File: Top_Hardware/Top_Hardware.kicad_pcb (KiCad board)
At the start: 2 copper layers, 15 parts, among them J1 NEO In, J2 Conn_01x03_Female

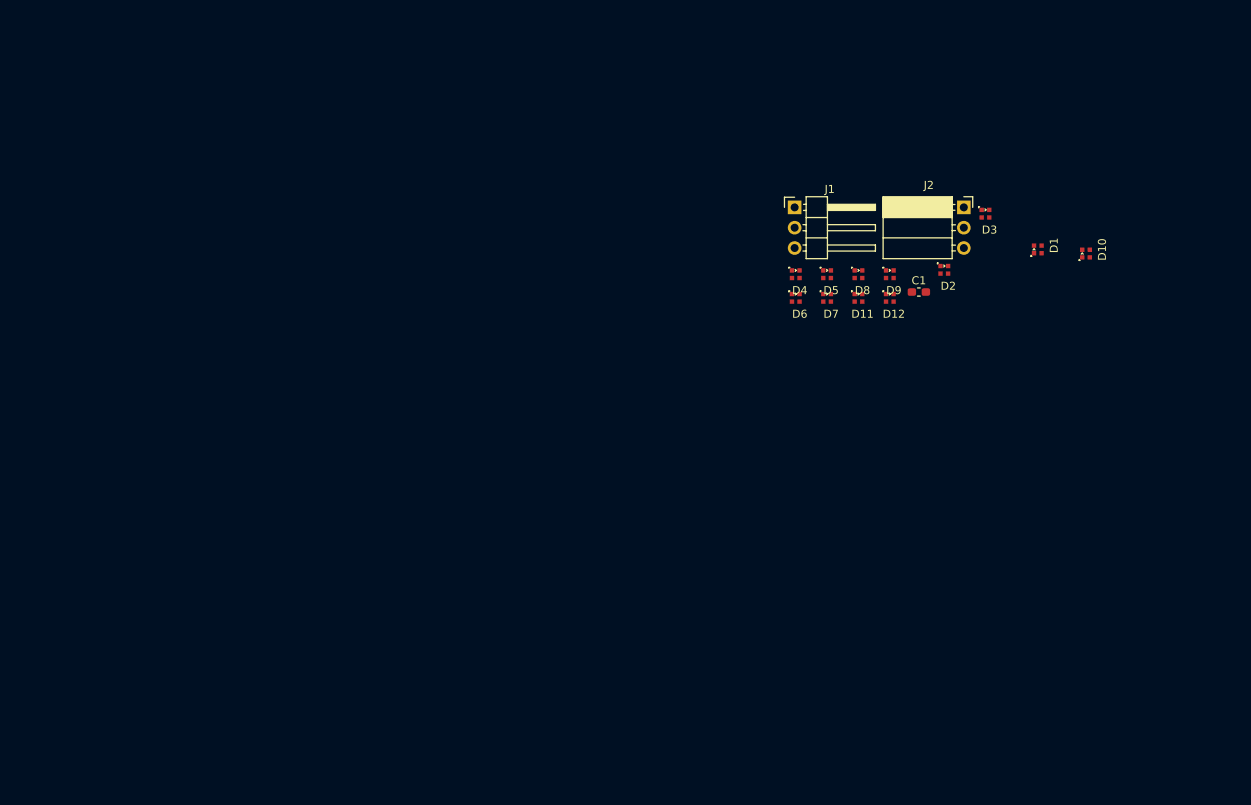
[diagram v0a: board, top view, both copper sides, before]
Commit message: created tree outlines
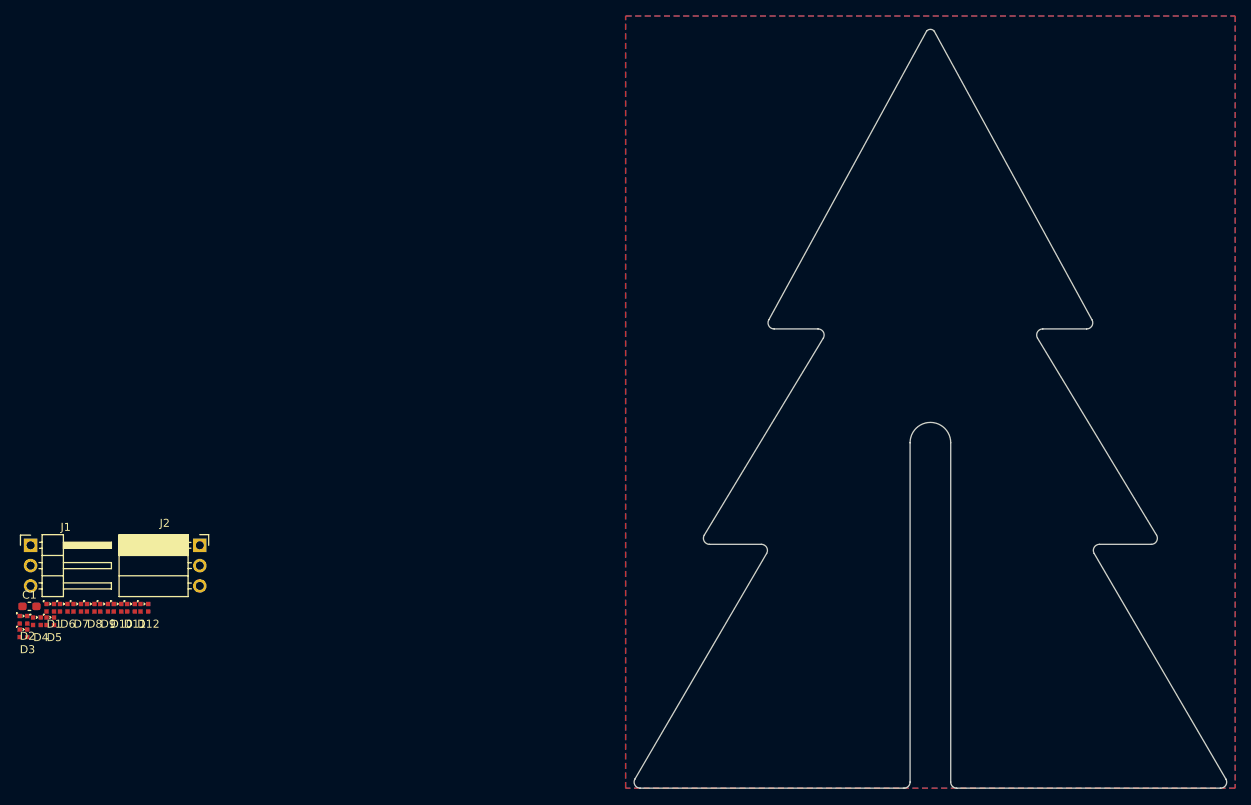
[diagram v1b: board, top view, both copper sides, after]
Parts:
- moved D1 131.3 mm to (32.2, 104.4), turned to 0 degrees
- moved D3 131.2 mm to (28.9, 107.6)
- moved D10 128.9 mm to (40.6, 104.4), turned to 0 degrees
- moved D2 123.1 mm to (28.9, 106.0)
- moved C1 117.9 mm to (29.6, 104.3)
- moved D9 106.7 mm to (38.9, 104.4)
- moved D5 106.3 mm to (32.2, 106.1)
- moved D8 104.6 mm to (37.3, 104.4)
- moved J2 104.4 mm to (50.9, 96.6)
- moved J1 104.4 mm to (29.8, 96.6)
- moved D4 104.3 mm to (30.5, 106.1)
- moved D7 101.4 mm to (35.6, 104.4)
- moved D12 100.9 mm to (44.0, 104.4)
- moved D6 99.4 mm to (33.9, 104.4)
- moved D11 98.8 mm to (42.3, 104.4)
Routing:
- added copper zone on B.Cu, net +5V
- added copper zone on F.Cu, net GND
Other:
- board outline added: 74.1 x 94.8 mm

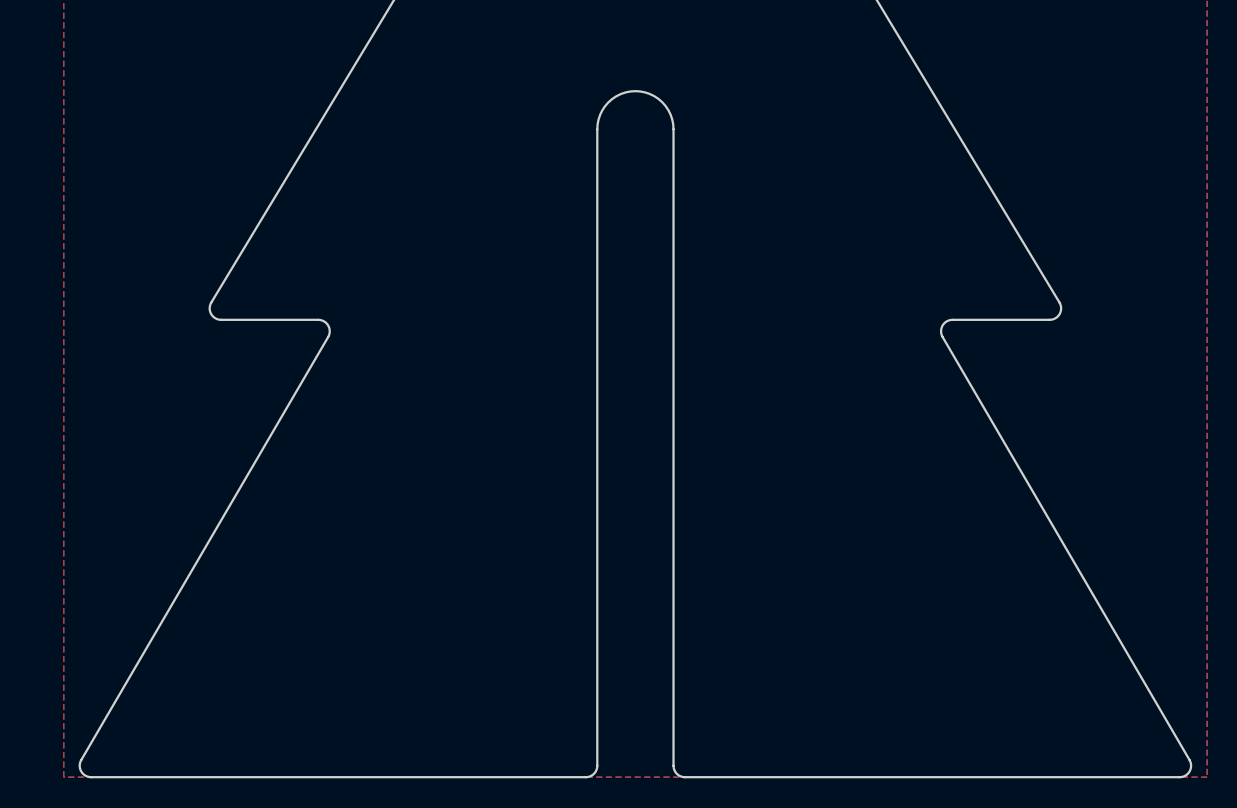
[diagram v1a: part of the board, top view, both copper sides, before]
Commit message: modified connecting slit
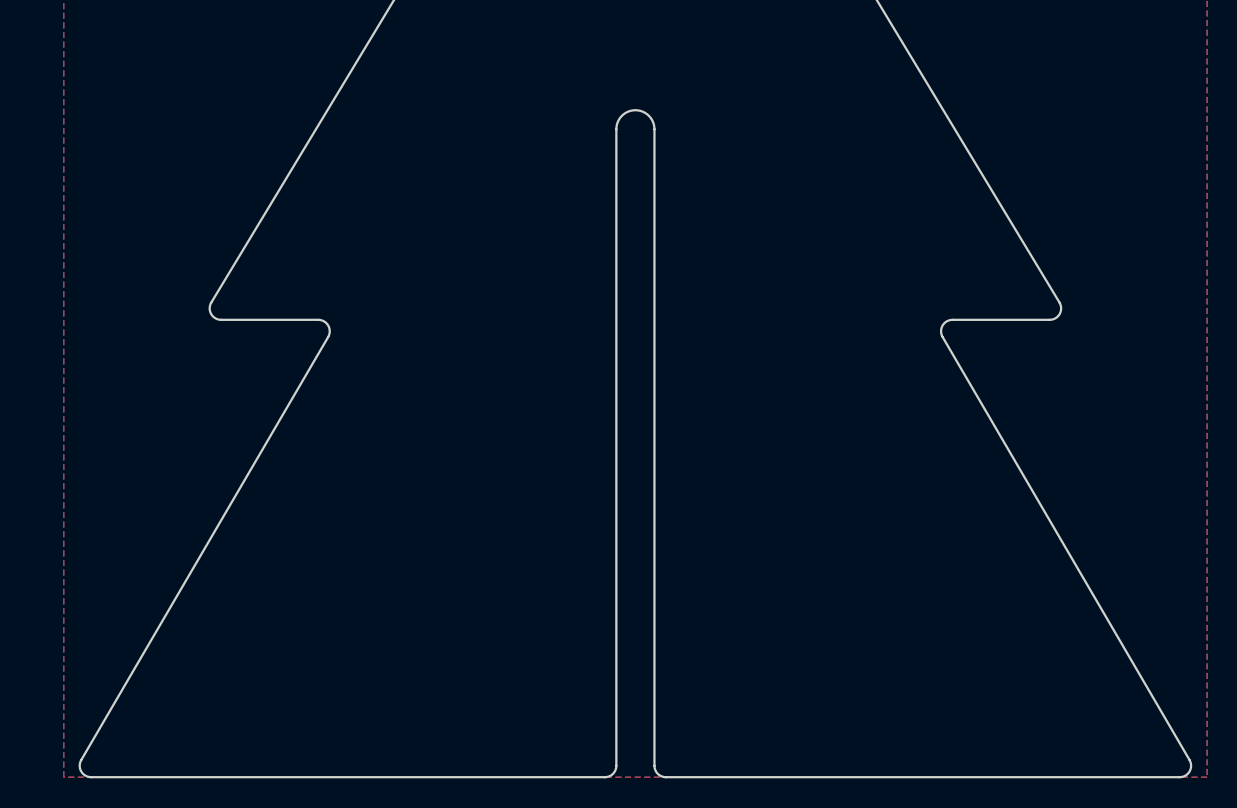
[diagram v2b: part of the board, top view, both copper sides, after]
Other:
- outline, holes or cut-outs redrawn
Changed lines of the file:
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@@
     )
   )
-  (gr_line (start 144.78 83.82) (end 144.78 126.238) (layer Edge.Cuts) (width 0.15))
-  (gr_line (start 145.542 127) (end 178.5112 127) (layer Edge.Cuts) (width 0.15))
-  (gr_arc (start 145.542 126.238) (end 145.542 127) (angle 90) (layer Edge.Cuts) (width 0.15))
-  (gr_arc (start 138.938 126.238) (end 138.938 127) (angle -90) (layer Edge.Cuts) (width 0.15))
-  (gr_line (start 138.938 127) (end 105.9688 127) (layer Edge.Cuts) (width 0.15))
-  (gr_line (start 139.7 83.82) (end 139.7 126.238) (layer Edge.Cuts) (width 0.15))
-  (gr_arc (start 142.24 83.82) (end 144.78 83.82) (angle -180) (layer Edge.Cuts) (width 0.15))
+  (gr_line (start 143.51 83.82) (end 143.51 126.238) (layer Edge.Cuts) (width 0.15))
+  (gr_line (start 144.272 127) (end 178.5112 127) (layer Edge.Cuts) (width 0.15))
+  (gr_arc (start 144.272 126.238) (end 144.272 127) (angle 90) (layer Edge.Cuts) (width 0.15))
+  (gr_arc (start 140.208 126.238) (end 140.208 127) (angle -90) (layer Edge.Cuts) (width 0.15))
+  (gr_line (start 140.208 127) (end 105.9688 127) (layer Edge.Cuts) (width 0.15))
+  (gr_line (start 140.97 83.82) (end 140.97 126.238) (layer Edge.Cuts) (width 0.15))
+  (gr_arc (start 142.24 83.82) (end 143.51 83.82) (angle -180) (layer Edge.Cuts) (width 0.15))
   (gr_arc (start 142.24 32.766) (end 142.7226 32.385) (angle -103.4196736) (layer Edge.Cuts) (width 0.15))
   (gr_line (start 128.8542 70.739) (end 113.9698 95.377) (layer Edge.Cuts) (width 0.15))

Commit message: Placed high-level components and traces
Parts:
- J1: footprint Connector_PinHeader_2.54mm:PinHeader_1x03_P2.54mm_Horizontal -> Connector_PinHeader_2.54mm:PinHeader_1x03_P2.54mm_Vertical; moved to B.Cu
- J2: footprint Connector_PinSocket_2.54mm:PinSocket_1x03_P2.54mm_Horizontal -> Connector_PinSocket_2.54mm:PinSocket_1x03_P2.54mm_Vertical; moved to B.Cu
- moved J1 108.9 mm to (138.4, 88.9), turned to 180 degrees
- moved J2 99.1 mm to (146.1, 124.5), turned to 270 degrees

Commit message: Finished layout
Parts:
- D10, D12, D2, D4, D6, D8: moved to B.Cu
- moved D11 135.6 mm to (176.4, 124.9), turned to 180 degrees
- moved D12 134.0 mm to (176.4, 124.9), turned to 270 degrees
- moved D7 129.0 mm to (159.2, 67.8), turned to 180 degrees
- moved D9 128.9 mm to (167.5, 94.5), turned to 180 degrees
- moved D8 127.3 mm to (159.2, 67.8), turned to 270 degrees
- moved D10 127.2 mm to (167.5, 94.4), turned to 270 degrees
- moved C1 110.5 mm to (138.4, 85.0), turned to 90 degrees
- moved D5 100.0 mm to (124.6, 67.8), turned to 90 degrees
- moved D6 97.8 mm to (124.6, 67.8), turned to 180 degrees
- moved D3 89.1 mm to (117.0, 94.5), turned to 90 degrees
- moved D4 87.2 mm to (117.0, 94.4), turned to 180 degrees
- moved D2 81.5 mm to (108.1, 124.9), turned to 180 degrees
- moved D1 78.6 mm to (108.1, 124.9), turned to 90 degrees
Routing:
- net /DIn: track 0.00 -> 62.4 mm, vias 0 -> 1
- net Net-(D10-Pad1): track 0.00 -> 48.1 mm, vias 0 -> 3
- net Net-(D2-Pad1): track 0.00 -> 48.1 mm, vias 0 -> 3
- net Net-(D8-Pad1): track 0.00 -> 42.0 mm, vias 0 -> 3
- net Net-(D4-Pad1): track 0.00 -> 42.0 mm, vias 0 -> 3
- net Net-(D6-Pad1): track 0.00 -> 34.5 mm, vias 0 -> 1
- net /DOut: track 0.00 -> 28.8 mm, vias 0 -> 1
- net +5V: track 0.00 -> 13.4 mm, vias 0 -> 6
- net GND: track 0.00 -> 9.39 mm, vias 0 -> 6
- net Net-(D5-Pad1): track 0.00 -> 3.71 mm, vias 0 -> 1
- net Net-(D11-Pad1): track 0.00 -> 3.38 mm, vias 0 -> 1
- net Net-(D7-Pad1): track 0.00 -> 2.94 mm, vias 0 -> 1
- net Net-(D10-Pad3): track 0.00 -> 2.94 mm, vias 0 -> 1
- net Net-(D3-Pad1): track 0.00 -> 2.89 mm, vias 0 -> 1
- net Net-(D1-Pad1): track 0.00 -> 2.89 mm, vias 0 -> 1
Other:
- board text added: "R1"
